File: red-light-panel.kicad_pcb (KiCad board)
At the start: 2 copper layers, 0 parts

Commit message: PCB fab rules: 2-layer 1oz/1oz, JLCPCB standard service + margin
- kicad_pcb: explicit stackup (1oz/1oz copper, 1.53mm FR4 core, 1.6mm
  overall, ENIG finish -- flagged upgrade from JLC's HASL default given
  this board's 0.4mm-pitch QFN parts).
- kicad_pro design rules: track width/clearance 0.15mm (6mil, ~1.7x
  JLCPCB's 3.5mil minimum), hole-to-copper 0.3mm, hole-to-hole 0.5mm,
  silk line/clearance 0.15mm, min text height 1.0mm -- every constraint
  set with margin above JLCPCB's published standard-service minimum, not
  at the limit.
- red-light-panel.kicad_dru: net-specific high-current trace-width
  overrides (1-1.5mm) for VBAT/VBAT_PROT/GND/USB_VBUS/LED channel/
  switching-node nets -- the board-wide 0.15mm minimum is nowhere near
  adequate for the ~5A-class currents in this design.
- docs/pcb_fabrication_rules.md: full value table + rationale.

kicad-cli pcb drc confirms the new rule files load and apply correctly
(caught a real issue: U2's WQFN-38 footprint has 0.2mm thermal vias,
below the new 0.3mm minimum -- flagged in the doc). Board still has all
153 footprints only default-imported, not placed/routed -- the several
hundred other DRC violations are all attributable to that pre-existing
state (overlapping placement, no board outline, pads not net-synced),
not to the new rules; layout remains a separate future step.

Co-Authored-By: Claude Sonnet 5 <noreply@anthropic.com>
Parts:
- added BT1: INR18650-30Q, Battery:BatteryHolder_Keystone_1042_1x18650, F.Cu at (102.5, 28.4)
- added BT2: INR18650-30Q, Battery:BatteryHolder_Keystone_1042_1x18650, F.Cu at (102.5, 51.1)
- added BT3: INR18650-30Q, Battery:BatteryHolder_Keystone_1042_1x18650, F.Cu at (102.5, 73.8)
- added BT4: INR18650-30Q, Battery:BatteryHolder_Keystone_1042_1x18650, F.Cu at (102.5, 96.5)
- added BT5: INR18650-30Q, Battery:BatteryHolder_Keystone_1042_1x18650, F.Cu at (102.5, 119.2)
- added BT6: INR18650-30Q, Battery:BatteryHolder_Keystone_1042_1x18650, F.Cu at (102.5, 141.9)
- added BT7: INR18650-30Q, Battery:BatteryHolder_Keystone_1042_1x18650, F.Cu at (102.5, 164.6)
- added BT8: INR18650-30Q, Battery:BatteryHolder_Keystone_1042_1x18650, F.Cu at (102.5, 187.3)
- added C1: 10uF, Capacitor_SMD:C_1206_3216Metric, F.Cu at (176.7, 122.4)
- added C10: 0.1uF, Capacitor_SMD:C_0603_1608Metric, F.Cu at (187.5, 64.5)
- added C11: 0.1uF, Capacitor_SMD:C_0603_1608Metric, F.Cu at (187.5, 67.0)
- added C12: 10uF, Capacitor_SMD:C_1206_3216Metric, F.Cu at (168.7, 69.6)
- added C13: 10uF, Capacitor_SMD:C_1206_3216Metric, F.Cu at (168.7, 73.0)
- added C14: 0.1uF, Capacitor_SMD:C_0603_1608Metric, F.Cu at (167.9, 86.8)
- added C15: 0.1uF, Capacitor_SMD:C_0603_1608Metric, F.Cu at (167.9, 89.3)
- added C16: 0.1uF, Capacitor_SMD:C_0603_1608Metric, F.Cu at (167.9, 91.8)
- added C17: 0.1uF, Capacitor_SMD:C_0603_1608Metric, F.Cu at (167.9, 94.3)
- added C18: 4.7uF, Capacitor_SMD:C_1206_3216Metric, F.Cu at (177.3, 107.0)
- added C2: 10uF, Capacitor_SMD:C_1206_3216Metric, F.Cu at (176.7, 125.7)
- added C3: 0.1uF, Capacitor_SMD:C_0603_1608Metric, F.Cu at (181.5, 122.0)
- added C4: 0.1uF, Capacitor_SMD:C_0603_1608Metric, F.Cu at (181.5, 124.5)
- added C5: 0.1uF, Capacitor_SMD:C_0603_1608Metric, F.Cu at (181.5, 127.0)
- added C6: 10uF, Capacitor_SMD:C_1206_3216Metric, F.Cu at (180.6, 136.9)
- added C7: 10uF, Capacitor_SMD:C_1206_3216Metric, F.Cu at (180.6, 140.3)
- added C8: 0.1uF, Capacitor_SMD:C_0603_1608Metric, F.Cu at (187.5, 59.5)
- added C9: 0.1uF, Capacitor_SMD:C_0603_1608Metric, F.Cu at (187.5, 62.0)
- added C90: 1uF (added, flagged), Capacitor_SMD:C_0603_1608Metric, F.Cu at (148.9, 77.0)
- added C91: 0.1uF (added, flagged), Capacitor_SMD:C_0603_1608Metric, F.Cu at (148.9, 79.5)
- added C92: 1uF (added, flagged -- PMID bulk cap per typical app circui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, Capacitor_SMD:C_1206_3216Metric, F.Cu at (176.7, 129.1)
- added C93: 2.2nF (added, flagged -- VBST bootstrap cap), Capacitor_SMD:C_0603_1608Metric, F.Cu at (185.4, 141.1)
- added C94: 100pF (added, flagged -- COFF timing, calc vs L freq), Capacitor_SMD:C_0603_1608Metric, F.Cu at (187.5, 69.5)
- added C95: 100pF (added, flagged -- COFF timing, calc vs L freq), Capacitor_SMD:C_0603_1608Metric, F.Cu at (191.5, 59.5)
- added D1: SMAJ24CA, Diode_SMD:D_SMA, F.Cu at (151.0, 73.5)
- added D10: SST-10-DR-B130-K660, red-light-panel:LUMINUS_SST-10-3535, F.Cu at (167.7, 37.4)
- added D11: SST-10-DR-B130-K660, red-light-panel:LUMINUS_SST-10-3535, F.Cu at (167.7, 41.0)
- added D12: SST-10-DR-B130-K660, red-light-panel:LUMINUS_SST-10-3535, F.Cu at (167.7, 44.8)
- added D13: SST-10-DR-B130-K660, red-light-panel:LUMINUS_SST-10-3535, F.Cu at (171.4, 18.9)
- added D14: SST-10-DR-B130-K660, red-light-panel:LUMINUS_SST-10-3535, F.Cu at (171.4, 22.6)
- added D15: SST-10-DR-B130-K660, red-light-panel:LUMINUS_SST-10-3535, F.Cu at (171.4, 26.2)
- added D16: SST-10-DR-B130-K660, red-light-panel:LUMINUS_SST-10-3535, F.Cu at (171.4, 29.9)
- added D17: SST-10-DR-B130-K660, red-light-panel:LUMINUS_SST-10-3535, F.Cu at (171.4, 33.6)
- added D18: SST-10-DR-B130-K660, red-light-panel:LUMINUS_SST-10-3535, F.Cu at (171.4, 37.4)
- added D19: SST-10-DR-B130-K660, red-light-panel:LUMINUS_SST-10-3535, F.Cu at (171.4, 41.0)
- added D2: TPD4S012DRYR (corrected from BOM's TPD4S012DBVR -- flag), Package_SON:Texas_USON-6_1x1.45mm_P0.5mm_SMD, F.Cu at (185.0, 122.4)
- added D20: SST-10-DR-B130-K660, red-light-panel:LUMINUS_SST-10-3535, F.Cu at (171.4, 44.8)
- added D21: SST-10-DR-B130-K660, red-light-panel:LUMINUS_SST-10-3535, F.Cu at (175.1, 18.9)
- added D22: SST-10-DR-B130-K660, red-light-panel:LUMINUS_SST-10-3535, F.Cu at (175.1, 22.6)
- added D23: SST-10-DR-B130-K660, red-light-panel:LUMINUS_SST-10-3535, F.Cu at (175.1, 26.2)
- added D24: SST-10-DR-B130-K660, red-light-panel:LUMINUS_SST-10-3535, F.Cu at (175.1, 29.9)
- added D25: SST-10-DR-B130-K660, red-light-panel:LUMINUS_SST-10-3535, F.Cu at (175.1, 33.6)
- added D26: SST-10-DR-B130-K660, red-light-panel:LUMINUS_SST-10-3535, F.Cu at (175.1, 37.4)
- added D27: SST-10-DR-B130-K660, red-light-panel:LUMINUS_SST-10-3535, F.Cu at (175.1, 41.0)
- added D28: SST-10-DR-B130-K660, red-light-panel:LUMINUS_SST-10-3535, F.Cu at (175.1, 44.8)
- added D29: SST-10-DR-B130-K660, red-light-panel:LUMINUS_SST-10-3535, F.Cu at (178.8, 18.9)
- added D3: SS54, Diode_SMD:D_SMA, F.Cu at (179.8, 76.6)
- added D30: SST-10-DR-B130-K660, red-light-panel:LUMINUS_SST-10-3535, F.Cu at (178.8, 22.6)
- added D31: SST-10-DR-B130-K660, red-light-panel:LUMINUS_SST-10-3535, F.Cu at (178.8, 26.2)
- added D32: SST-10-DR-B130-K660, red-light-panel:LUMINUS_SST-10-3535, F.Cu at (178.8, 29.9)
- added D33: SST-10-DR-B130-K660, red-light-panel:LUMINUS_SST-10-3535, F.Cu at (178.8, 33.6)
- added D34: SST-10-DR-B130-K660, red-light-panel:LUMINUS_SST-10-3535, F.Cu at (178.8, 37.4)
- added D35: SST-10-DR-B130-K660, red-light-panel:LUMINUS_SST-10-3535, F.Cu at (178.8, 41.0)
- added D36: SST-10-DR-B130-K660, red-light-panel:LUMINUS_SST-10-3535, F.Cu at (178.8, 44.8)
- added D37: SST-10-DR-B130-K660, red-light-panel:LUMINUS_SST-10-3535, F.Cu at (182.5, 18.9)
- added D38: SST-10-DR-B130-K660, red-light-panel:LUMINUS_SST-10-3535, F.Cu at (182.5, 22.6)
- added D39: SST-10-DR-B130-K660, red-light-panel:LUMINUS_SST-10-3535, F.Cu at (182.5, 26.2)
- added D4: SS54, Diode_SMD:D_SMA, F.Cu at (179.8, 81.1)
- added D40: SST-10-DR-B130-K660, red-light-panel:LUMINUS_SST-10-3535, F.Cu at (182.5, 29.9)
- added D41: SST-10-DR-B130-K660, red-light-panel:LUMINUS_SST-10-3535, F.Cu at (182.5, 33.6)
- added D42: SST-10-DR-B130-K660, red-light-panel:LUMINUS_SST-10-3535, F.Cu at (182.5, 37.4)
- added D43: SST-10-DR-B130-K660, red-light-panel:LUMINUS_SST-10-3535, F.Cu at (182.5, 41.0)
- added D44: SST-10-DR-B130-K660, red-light-panel:LUMINUS_SST-10-3535, F.Cu at (182.5, 44.8)
- added D45: SST-10-DR-B130-K660, red-light-panel:LUMINUS_SST-10-3535, F.Cu at (186.2, 18.9)
- added D46: SST-10-DR-B130-K660, red-light-panel:LUMINUS_SST-10-3535, F.Cu at (186.2, 22.6)
- added D47: SST-10-DR-B130-K660, red-light-panel:LUMINUS_SST-10-3535, F.Cu at (186.2, 26.2)
- added D48: SST-10-DR-B130-K660, red-light-panel:LUMINUS_SST-10-3535, F.Cu at (186.2, 29.9)
- added D49: SST-10-DR-B130-K660, red-light-panel:LUMINUS_SST-10-3535, F.Cu at (186.2, 33.6)
- added D5: SST-10-DR-B130-K660, red-light-panel:LUMINUS_SST-10-3535, F.Cu at (167.7, 18.9)
- added D50: SST-10-DR-B130-K660, red-light-panel:LUMINUS_SST-10-3535, F.Cu at (186.2, 37.4)
- added D51: SST-10-DR-B130-K660, red-light-panel:LUMINUS_SST-10-3535, F.Cu at (186.2, 41.0)
- added D52: SST-10-DR-B130-K660, red-light-panel:LUMINUS_SST-10-3535, F.Cu at (186.2, 44.8)
- added D53: SST-10-DR-B130-K660, red-light-panel:LUMINUS_SST-10-3535, F.Cu at (189.9, 18.9)
- added D54: SST-10-DR-B130-K660, red-light-panel:LUMINUS_SST-10-3535, F.Cu at (189.9, 22.6)
- added D55: SST-10-DR-B130-K660, red-light-panel:LUMINUS_SST-10-3535, F.Cu at (189.9, 26.2)
- added D56: SST-10-DR-B130-K660, red-light-panel:LUMINUS_SST-10-3535, F.Cu at (189.9, 29.9)
- added D57: SST-10-DR-B130-K660, red-light-panel:LUMINUS_SST-10-3535, F.Cu at (189.9, 33.6)
- added D58: SST-10-DR-B130-K660, red-light-panel:LUMINUS_SST-10-3535, F.Cu at (189.9, 37.4)
- added D59: SST-10-DR-B130-K660, red-light-panel:LUMINUS_SST-10-3535, F.Cu at (189.9, 41.0)
- added D6: SST-10-DR-B130-K660, red-light-panel:LUMINUS_SST-10-3535, F.Cu at (167.7, 22.6)
- added D60: SST-10-DR-B130-K660, red-light-panel:LUMINUS_SST-10-3535, F.Cu at (189.9, 44.8)
- added D61: SST-10-DR-B130-K660, red-light-panel:LUMINUS_SST-10-3535, F.Cu at (193.6, 18.9)
- added D62: SST-10-DR-B130-K660, red-light-panel:LUMINUS_SST-10-3535, F.Cu at (193.6, 22.6)
- added D63: SST-10-DR-B130-K660, red-light-panel:LUMINUS_SST-10-3535, F.Cu at (193.6, 26.2)
- added D64: SST-10-DR-B130-K660, red-light-panel:LUMINUS_SST-10-3535, F.Cu at (193.6, 29.9)
- added D65: SST-10-DR-B130-K660, red-light-panel:LUMINUS_SST-10-3535, F.Cu at (193.6, 33.6)
- added D66: SST-10-DR-B130-K660, red-light-panel:LUMINUS_SST-10-3535, F.Cu at (193.6, 37.4)
- added D67: SST-10-DR-B130-K660, red-light-panel:LUMINUS_SST-10-3535, F.Cu at (193.6, 41.0)
- added D68: SST-10-DR-B130-K660, red-light-panel:LUMINUS_SST-10-3535, F.Cu at (193.6, 44.8)
- added D69: TPD4E001DBVR (corrected from BOM's TPD4E001DZDR -- flag), Package_TO_SOT_SMD:SOT-23-6, F.Cu at (186.7, 99.4)
- added D7: SST-10-DR-B130-K660, red-light-panel:LUMINUS_SST-10-3535, F.Cu at (167.7, 26.2)
- added D70: TPD4E001DBVR (corrected from BOM's TPD4E001DZDR -- flag), Package_TO_SOT_SMD:SOT-23-6, F.Cu at (186.7, 104.0)
- added D71: APT1608LSECK/J4-PRV (single-color, corrected per your decis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, LED_SMD:LED_0603_1608Metric, F.Cu at (173.8, 149.1)
- added D8: SST-10-DR-B130-K660, red-light-panel:LUMINUS_SST-10-3535, F.Cu at (167.7, 29.9)
- added D9: SST-10-DR-B130-K660, red-light-panel:LUMINUS_SST-10-3535, F.Cu at (167.7, 33.6)
- added F1: 0.25A resettable, Fuse:Fuse_BelFuse_0ZRE0025FF_L9.6mm_W3.8mm, F.Cu at (150.0, 54.7)
- added J1: JST B5B-XH-A, Connector_JST:JST_XH_B5B-XH-A_1x05_P2.50mm_Vertical, F.Cu at (150.4, 20.4)
- added J2: Molex 43045-0200, Connector_Molex:Molex_Micro-Fit_3.0_43045-0200_2x01_P3.00mm_Horizontal, F.Cu at (151.5, 34.7)
- added J3: USB4105-GF-A (plating/stake length TBD, flag), Connector_USB:USB_C_Receptacle_GCT_USB4105-xx-A_16P_TopMnt_Horizontal, F.Cu at (171.7, 116.0)
- added J4: 2-pin screw terminal / JST-PH-2, Connector_JST:JST_PH_S2B-PH-K_1x02_P2.00mm_Horizontal, F.Cu at (168.9, 49.0)
- added J5: 2-pin screw terminal / JST-PH-2, Connector_JST:JST_PH_S2B-PH-K_1x02_P2.00mm_Horizontal, F.Cu at (176.8, 49.0)
- added J6: Cortex Debug 10-pin, Connector_PinHeader_1.27mm:PinHeader_2x05_P1.27mm_Vertical_SMD, F.Cu at (179.3, 101.2)
- added J7: Debug breakout (SWDIO,SWCLK,NRST,3.3V,GND), Connector_PinHeader_2.54mm:PinHeader_1x05_P2.54mm_Vertical, F.Cu at (172.2, 87.8)
- added L1: 2.2uH (Wurth 744031220), Inductor_SMD:L_Vishay_IFSC-1515AH_4x4x1.8mm, F.Cu at (180.6, 144.7)
- added L2: IHLP2525CZERR10M01 (0.10uH), Inductor_SMD:L_Vishay_IHLP-2525, F.Cu at (180.6, 62.3)
- added L3: IHLP2525CZERR10M01 (0.10uH), Inductor_SMD:L_Vishay_IHLP-2525, F.Cu at (180.6, 70.3)
- added L90: 2.2uH (added, flagged -- calc vs target charge current), Inductor_SMD:L_Vishay_IHLP-2525, F.Cu at (182.5, 114.7)
- added Q1: CSD18540Q5B, Package_TO_SOT_SMD:TDSON-8-1, F.Cu at (151.0, 42.9)
- added Q2: CSD18540Q5B, Package_TO_SOT_SMD:TDSON-8-1, F.Cu at (151.0, 49.6)
- added Q3: AO3401A, Package_TO_SOT_SMD:SOT-23, F.Cu at (153.4, 78.0)
- added Q4: AO3401A (30V Vds, satisfies brief's margin flag), Package_TO_SOT_SMD:SOT-23, F.Cu at (168.3, 76.9)
- added Q5: AO3401A (30V Vds, satisfies brief's margin flag), Package_TO_SOT_SMD:SOT-23, F.Cu at (168.3, 81.3)
- added R1: 0.01R 1%, Resistor_SMD:R_Shunt_Vishay_WSK2512_6332Metric_T2.21mm, F.Cu at (151.8, 60.7)
- added R10: 10k, Resistor_SMD:R_0603_1608Metric, F.Cu at (173.7, 139.0)
- added R11: 10k, Resistor_SMD:R_0603_1608Metric, F.Cu at (173.7, 141.5)
- added R12: 10k, Resistor_SMD:R_0603_1608Metric, F.Cu at (173.7, 144.0)
- added R13: 680R (calc vs Vf/If, flag), Resistor_SMD:R_0603_1608Metric, F.Cu at (173.7, 146.6)
- added R2: 10k, Resistor_SMD:R_0603_1608Metric, F.Cu at (185.4, 143.6)
- added R3: 3.01k (calc, flag), Resistor_SMD:R_0603_1608Metric, F.Cu at (185.4, 146.2)
- added R4: 0.02R 1%, Resistor_SMD:R_Shunt_Vishay_WSK2512_6332Metric_T2.21mm, F.Cu at (170.8, 60.7)
- added R5: 0.02R 1%, Resistor_SMD:R_Shunt_Vishay_WSK2512_6332Metric_T2.21mm, F.Cu at (170.8, 65.5)
- added R6: 10k, Resistor_SMD:R_0603_1608Metric, F.Cu at (167.9, 96.8)
- added R7: 10k, Resistor_SMD:R_0603_1608Metric, F.Cu at (167.9, 99.4)
- added R8: 10k, Resistor_SMD:R_0603_1608Metric, F.Cu at (167.9, 101.9)
- added R9: 10k, Resistor_SMD:R_0603_1608Metric, F.Cu at (173.7, 136.5)
- added R90: 100k, Resistor_SMD:R_0603_1608Metric, F.Cu at (148.9, 82.0)
- added R91: 10k (added, flagged -- ILIM_HIZ set resistor, calc per data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, Resistor_SMD:R_0603_1608Metric, F.Cu at (181.5, 129.5)
- added R92: 4.7k (added, flagged -- PROG set resistor, calc per datashe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, Resistor_SMD:R_0603_1608Metric, F.Cu at (181.5, 132.0)
- added R94: 100k (added, flagged -- COFF timing, calc vs L freq), Resistor_SMD:R_0603_1608Metric, F.Cu at (191.5, 62.0)
- added R95: 100k (added, flagged -- UVLO always-on pull-up, no set thre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, Resistor_SMD:R_0603_1608Metric, F.Cu at (191.5, 64.5)
- added R96: 100k (added, flagged -- COFF timing, calc vs L freq), Resistor_SMD:R_0603_1608Metric, F.Cu at (191.5, 67.0)
- added R97: 100k (added, flagged -- UVLO always-on pull-up, no set thre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, Resistor_SMD:R_0603_1608Metric, F.Cu at (191.5, 69.5)
- added R98: 10k (added, flagged -- NTC divider pull-up), Resistor_SMD:R_0603_1608Metric, F.Cu at (183.8, 47.9)
- added RT1: NCP18XH103F03RB (10k NTC), Resistor_SMD:R_0603_1608Metric, F.Cu at (183.8, 50.4)
- added SW1: Omron B3U-1000P, Button_Switch_SMD:SW_SPST_B3U-1000P, F.Cu at (168.8, 137.4)
- added SW2: Omron B3U-1000P, Button_Switch_SMD:SW_SPST_B3U-1000P, F.Cu at (168.8, 141.8)
- added SW3: Omron B3U-1000P, Button_Switch_SMD:SW_SPST_B3U-1000P, F.Cu at (168.8, 146.1)
- added SW4: Omron B3U-1000P, Button_Switch_SMD:SW_SPST_B3U-1000P, F.Cu at (168.8, 150.5)
- added U1: BQ76920PW, Package_SO:TSSOP-20_4.4x6.5mm_P0.65mm, F.Cu at (151.7, 67.2)
- added U2: TPS25751DREFR (active replacement for NRND TPS25750DRYR, pe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, Package_DFN_QFN:Texas_REF0038A_WQFN-38-2EP_6x4mm_P0.4, F.Cu at (169.9, 123.7)
- added U3: BQ25792RQMR, Package_DFN_QFN:Texas_RQM0029A_VQFN-29_4x4mm_P0.4mm, F.Cu at (169.2, 129.7)
- added U4: TPS563201DDCR, Package_TO_SOT_SMD:SOT-23-6, F.Cu at (186.0, 137.7)
- added U5: LM3409HVMY/NOPB, Package_SO:HVSSOP-10-1EP_3x3mm_P0.5mm_EP1.83x1.89mm, F.Cu at (187.4, 76.6)
- added U6: LM3409HVMY/NOPB, Package_SO:HVSSOP-10-1EP_3x3mm_P0.5mm_EP1.83x1.89mm, F.Cu at (187.4, 81.2)
- added U7: STM32G031K8T6, Package_QFP:LQFP-32_7x7mm_P0.8mm, F.Cu at (180.2, 91.3)
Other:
- rule pad_to_mask_clearance: 0 -> 0.05

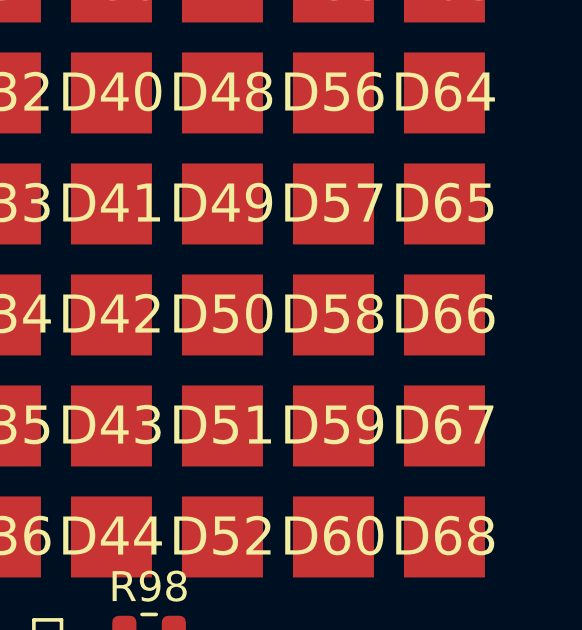
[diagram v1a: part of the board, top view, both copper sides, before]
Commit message: Reapply PCB fab rules (stackup + DRC margins) after GUI overwrite
The KiCad GUI was left open from an earlier session and silently reverted
the previous fab-rules commit (446f7ae) when it autosaved with its own
stale in-memory project state -- stackup was gone, DRC minimums were back
to KiCad's stock defaults. Closed KiCad first this time, then reapplied
the same values directly to the files on disk so nothing is open to
clobber them again. Same content as 446f7ae: 2-layer 1oz/1oz ENIG
stackup, 0.15mm track/clearance, 0.3mm hole clearance, 0.5mm hole-to-hole,
0.15mm silk clearance, 1.0mm min text height.

Note: the same GUI session also appears to have re-synced some PCB pads
to stale auto-generated net names (e.g. 'Net-(BT3-+)' instead of 'TAP2'),
independent of this fix -- worth re-running Update PCB from Schematic
once the schematic side is in its final state, since that's a separate
issue from the DRC-rules regression this commit addresses.

Co-Authored-By: Claude Sonnet 5 <noreply@anthropic.com>
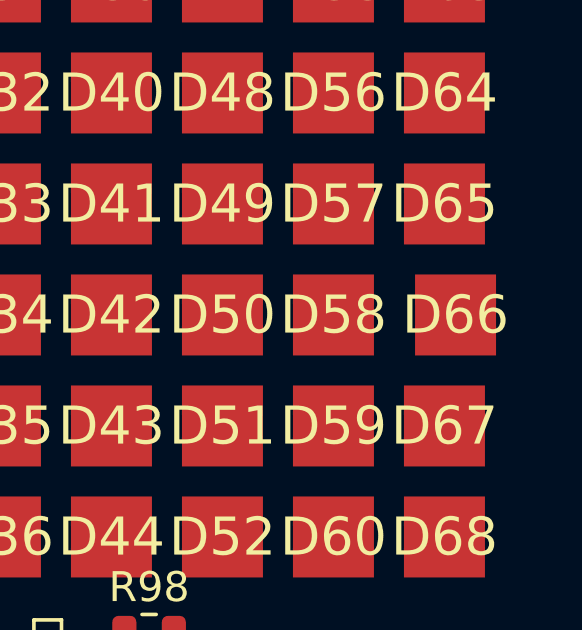
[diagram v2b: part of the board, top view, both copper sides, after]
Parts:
- moved D66 0.37 mm to (194.0, 37.4)
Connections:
- BT1 pad 1: TAP1 -> Net-(BT1-+)
- BT2 pad 1: TAP1 -> Net-(BT2-+)
- BT3 pad 1: TAP2 -> Net-(BT3-+)
- BT3 pad 2: TAP1 -> Net-(BT1-+)
- BT4 pad 1: TAP2 -> Net-(BT4-+)
- BT4 pad 2: TAP1 -> Net-(BT2-+)
- BT5 pad 1: TAP3 -> Net-(BT5-+)
- BT5 pad 2: TAP2 -> Net-(BT3-+)
- BT6 pad 1: TAP3 -> Net-(BT6-+)
- BT6 pad 2: TAP2 -> Net-(BT4-+)
- BT7 pad 2: TAP3 -> Net-(BT5-+)
- BT8 pad 2: TAP3 -> Net-(BT6-+)
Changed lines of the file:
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@@
 			(layers "F.Cu" "F.Mask" "F.Paste")
 			(roundrect_rratio 0.038462)
-			(net "TAP2")
+			(net "Net-(BT3-+)")
 			(pinfunction "+_1")
 			(pintype "passive")
@@
 			(layers "F.Cu" "F.Mask" "F.Paste")
 			(roundrect_rratio 0.038462)
-			(net "TAP1")
+			(net "Net-(BT1-+)")
 			(pinfunction "-_2")
 			(pintype "passive")
@@
 			(layers "F.Cu" "F.Mask" "F.Paste")
 			(roundrect_rratio 0.038462)
-			(net "TAP1")
+			(net "Net-(BT1-+)")
 			(pinfunction "+_1")
 			(pintype "passive")
@@
 			(layers "F.Cu" "F.Mask" "F.Paste")
 			(roundrect_rratio 0.038462)
-			(net "TAP1")
+			(net "Net-(BT2-+)")
 			(pinfunction "+_1")
 			(pintype "passive")
@@
 			(layers "F.Cu" "F.Mask" "F.Paste")
 			(roundrect_rratio 0.038462)
-			(net "TAP2")
+			(net "Net-(BT4-+)")
 			(pinfunction "+_1")
 			(pintype "passive")
@@
 			(layers "F.Cu" "F.Mask" "F.Paste")
 			(roundrect_rratio 0.038462)
-			(net "TAP1")
+			(net "Net-(BT2-+)")
 			(pinfunction "-_2")
 			(pintype "passive")
@@
 			(layers "F.Cu" "F.Mask" "F.Paste")
 			(roundrect_rratio 0.038462)
-			(net "TAP3")
+			(net "Net-(BT5-+)")
 			(pinfunction "-_2")
 			(pintype "passive")
@@
 			(layers "F.Cu" "F.Mask" "F.Paste")
 			(roundrect_rratio 0.038462)
-			(net "TAP3")
+			(net "Net-(BT6-+)")
 			(pinfunction "+_1")
 			(pintype "passive")
@@
 			(layers "F.Cu" "F.Mask" "F.Paste")
 			(roundrect_rratio 0.038462)
-			(net "TAP2")
+			(net "Net-(BT4-+)")
 			(pinfunction "-_2")
 			(pintype "passive")
@@
 			(layers "F.Cu" "F.Mask" "F.Paste")
 			(roundrect_rratio 0.038462)
-			(net "TAP3")
+			(net "Net-(BT6-+)")
 			(pinfunction "-_2")
 			(pintype "passive")
@@
 			(layers "F.Cu" "F.Mask" "F.Paste")
 			(roundrect_rratio 0.038462)
-			(net "TAP3")
+			(net "Net-(BT5-+)")
 			(pinfunction "+_1")
 			(pintype "passive")
@@
 			(layers "F.Cu" "F.Mask" "F.Paste")
 			(roundrect_rratio 0.038462)
-			(net "TAP2")
+			(net "Net-(BT3-+)")
 			(pinfunction "-_2")
 			(pintype "passive")
@@
 	(footprint "red-light-panel:LUMINUS_SST-10-3535"
 		(layer "F.Cu")
-		(at 193.63 37.35)
+		(at 194 37.35)
 		(descr "Luminus SST-10-DR 3535 SMD LED, 3-pad (anode / center thermal-only pad / cathode). Pad dims per datasheet mechanical drawing (~3.45x3.45mm body, 3 stacked ~2.7x1.0mm pads).")
 		(tags "LED Luminus SST-10 3535")
